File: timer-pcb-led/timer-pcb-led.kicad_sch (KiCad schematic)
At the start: 10 parts, among them J1 JST_03

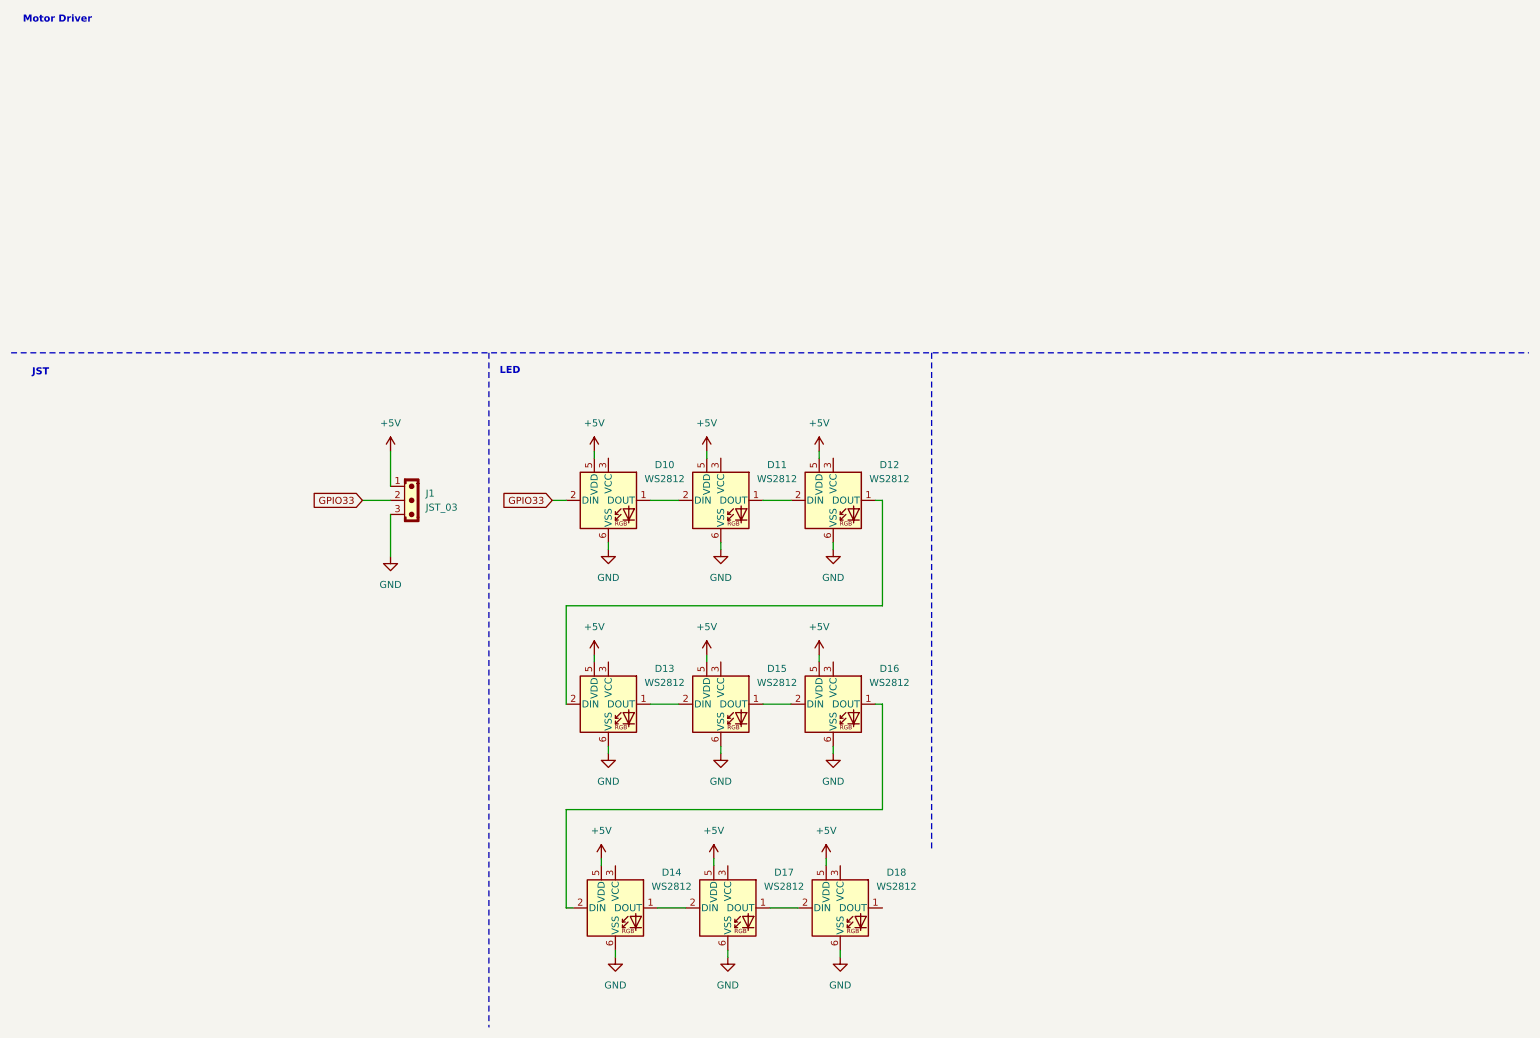
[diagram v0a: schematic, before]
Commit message: rework des PCB stepper et led. création du PCB chargeur
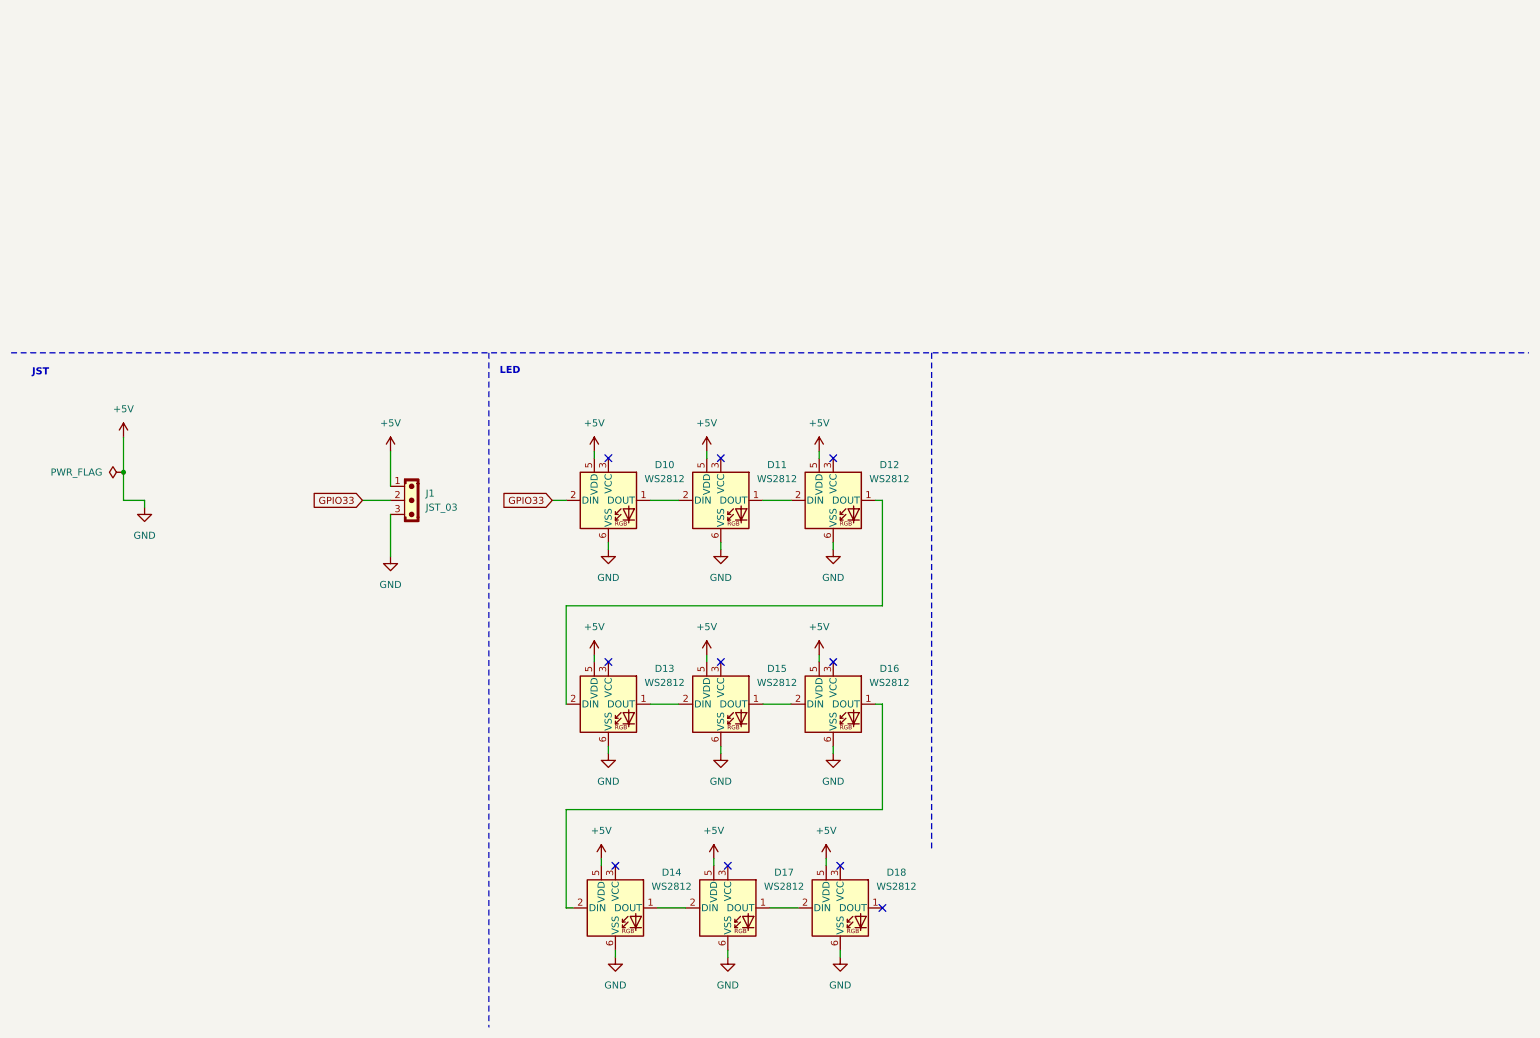
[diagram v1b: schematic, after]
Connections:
- net GND is gone; now on net +5V: D10.6 (VSS), D11.6 (VSS), D12.6 (VSS), D13.6 (VSS), D14.6 (VSS), D15.6 (VSS), D16.6 (VSS), D17.6 (VSS), D18.6 (VSS), J1.3
- no-connect marks 0 -> 10
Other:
- note removed: "Motor Driver"

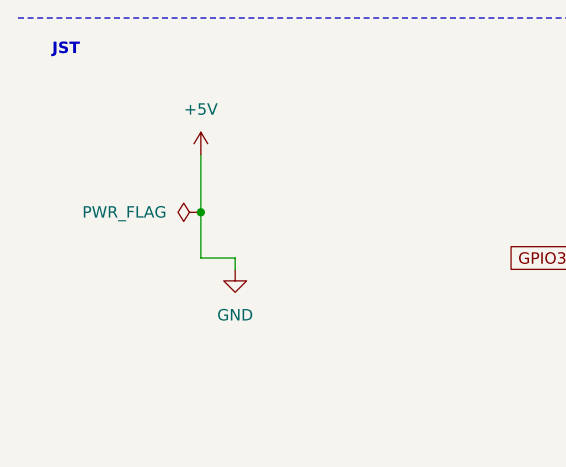
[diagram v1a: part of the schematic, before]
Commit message: mise à jour fichier kicad stepper + led. création dossier chargeur PCB.création du fichier .rpt
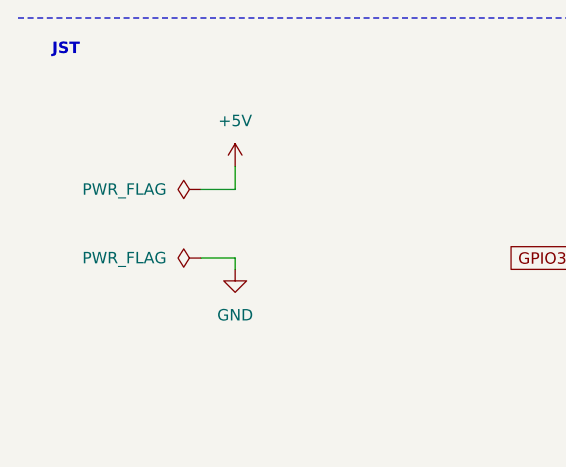
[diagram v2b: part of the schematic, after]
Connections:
- net +5V: no longer D10.6 (VSS), D11.6 (VSS), D12.6 (VSS), D13.6 (VSS), D14.6 (VSS), D15.6 (VSS), D16.6 (VSS), D17.6 (VSS), D18.6 (VSS), J1.3
- new net GND: D10.6 (VSS), D11.6 (VSS), D12.6 (VSS), D13.6 (VSS), D14.6 (VSS), D15.6 (VSS), D16.6 (VSS), D17.6 (VSS), D18.6 (VSS), J1.3
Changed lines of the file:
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@@
 		)
-	)
-	(junction
-		(at 31.75 97.79)
-		(diameter 0)
-		(color 0 0 0 0)
 	)
 	(no_connect
@@
 	(wire
 		(pts
-			(xy 31.75 102.87) (xy 31.75 97.79)
-		)
-		(stroke
-			(width 0)
-			(type default)
-		)
-	)
-	(wire
-		(pts
 			(xy 116.84 130.81) (xy 116.84 132.08)
 		)
@@
 	(wire
 		(pts
+			(xy 35.56 95.25) (xy 31.75 95.25)
+		)
+		(stroke
+			(width 0)
+			(type default)
+		)
+	)
+	(wire
+		(pts
 			(xy 147.32 102.87) (xy 152.4 102.87)
 		)
@@
 	(wire
 		(pts
-			(xy 31.75 91.44) (xy 31.75 97.79)
+			(xy 35.56 92.71) (xy 35.56 95.25)
 		)
 		(stroke
@@
 	(symbol
 		(lib_id "power:+5V")
-		(at 31.75 91.44 0)
+		(at 35.56 92.71 0)
 		(unit 1)
 		(exclude_from_sim no)
@@
 		(fields_autoplaced yes)
 		(property "Reference" "#PWR016"
-			(at 31.75 95.25 0)
+			(at 35.56 96.52 0)
 			(effects
 				(font
@@
 		)
 		(property "Value" "+5V"
-			(at 31.75 86.36 0)
+			(at 35.56 87.63 0)
 			(effects
 				(font
@@
 		)
 		(property "Footprint" ""
-			(at 31.75 91.44 0)
+			(at 35.56 92.71 0)
 			(effects
 				(font
@@
 		)
 		(property "Datasheet" ""
-			(at 31.75 91.44 0)
+			(at 35.56 92.71 0)
 			(effects
 				(font
@@
 		)
 		(property "Description" "Power symbol creates a global label with name \"+5V\""
-			(at 31.75 91.44 0)
+			(at 35.56 92.71 0)
 			(effects
 				(font
@@
 	)
 	(symbol
+		(lib_id "power:PWR_FLAG")
+		(at 31.75 102.87 90)
+		(unit 1)
+		(exclude_from_sim no)
+		(in_bom yes)
+		(on_board yes)
+		(dnp no)
+		(fields_autoplaced yes)
+		(property "Reference" "#FLG02"
+			(at 29.845 102.87 0)
+			(effects
+				(font
+					(size 1.27 1.27)
+				)
+				(hide yes)
+			)
+		)
+		(property "Value" "PWR_FLAG"
+			(at 27.94 102.8699 90)
+			(effects
+				(font
+					(size 1.27 1.27)
+				)
+				(justify left)
+			)
+		)
+		(property "Footprint" ""
+			(at 31.75 102.87 0)
+			(effects
+				(font
+					(size 1.27 1.27)
+				)
+				(hide yes)
+			)
+		)
+		(property "Datasheet" "~"
+			(at 31.75 102.87 0)
+			(effects
+				(font
+					(size 1.27 1.27)
+				)
+				(hide yes)
+			)
+		)
+		(property "Description" "Special symbol for telling ERC where power comes from"
+			(at 31.75 102.87 0)
+			(effects
+				(font
+					(size 1.27 1.27)
+				)
+				(hide yes)
+			)
+		)
+		(pin "1"
+		)
+		(instances
+			(project "timer-pcb-led"
+				(path "/c4cfdf40-c3b2-4c58-998c-a7d7b70b9691"
+					(reference "#FLG02")
+					(unit 1)
+				)
+			)
+		)
+	)
+	(symbol
 		(lib_id "power:GND")
 		(at 119.38 111.76 0)
@@
 	(symbol
 		(lib_id "power:PWR_FLAG")
-		(at 31.75 97.79 90)
+		(at 31.75 95.25 90)
 		(unit 1)
 		(exclude_from_sim no)
@@
 		(fields_autoplaced yes)
 		(property "Reference" "#FLG01"
-			(at 29.845 97.79 0)
+			(at 29.845 95.25 0)
 			(effects
 				(font
@@
 		)
 		(property "Value" "PWR_FLAG"
-			(at 27.94 97.7899 90)
+			(at 27.94 95.2499 90)
 			(effects
 				(font
@@
 		)
 		(property "Footprint" ""
-			(at 31.75 97.79 0)
+			(at 31.75 95.25 0)
 			(effects
 				(font
@@
 		)
 		(property "Datasheet" "~"
-			(at 31.75 97.79 0)
+			(at 31.75 95.25 0)
 			(effects
 				(font
@@
 		)
 		(property "Description" "Special symbol for telling ERC where power comes from"
-			(at 31.75 97.79 0)
-			(effects
-				(font
+			(at 31.75 95.25 0)
+			(effects
+				(font
